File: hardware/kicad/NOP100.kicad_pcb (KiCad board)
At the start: 4 copper layers, 100 x 85 mm, 51 parts, among them CON1 MIKROBUS MODULE 0, CON2 MIKROBUS MODULE 1, J1 CAN, Q1 BSS138, Q2 BSS138, SW1 BUS, SW2 SW_Push, U1 NCS1S1205SC, U2 MCP2551-I-P, U3 Teensy_4.0, U4 74HC165, U6 NCS1S1203SC

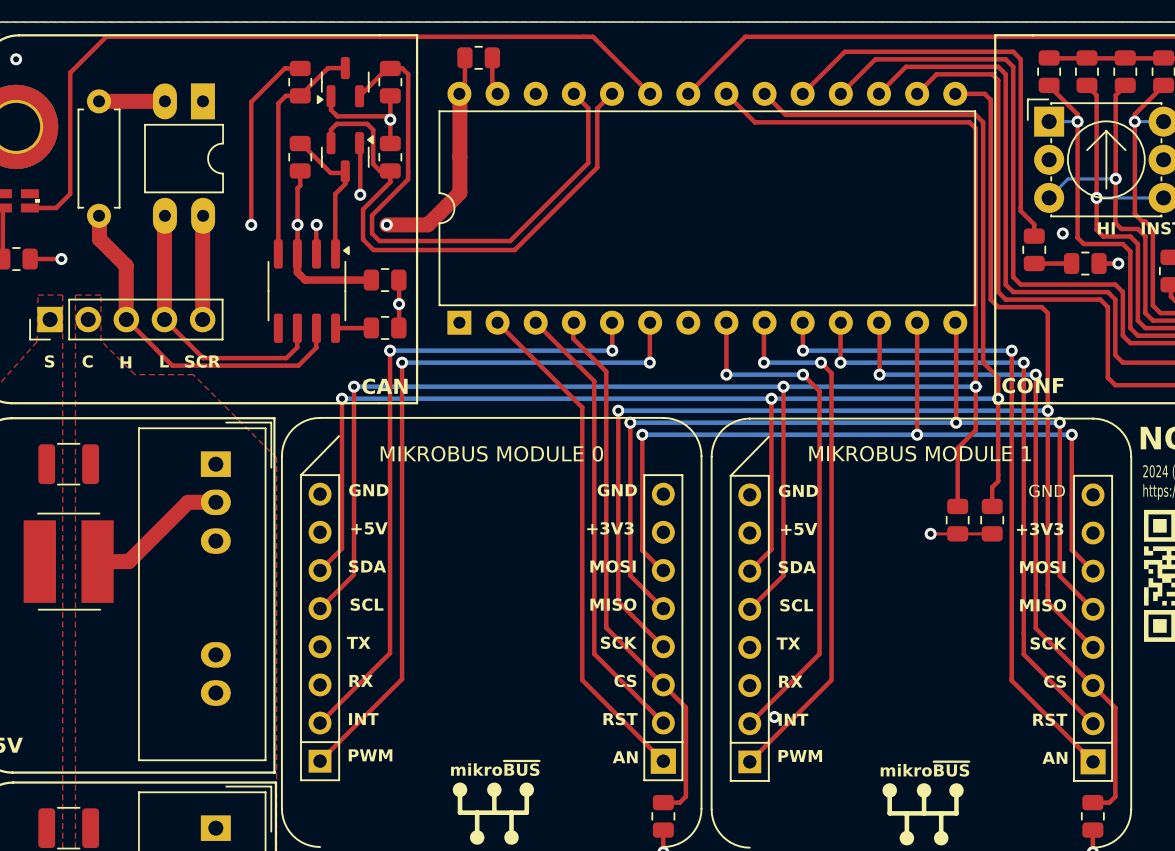
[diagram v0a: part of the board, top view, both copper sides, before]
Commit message: Add 3.3VDC alternatives.
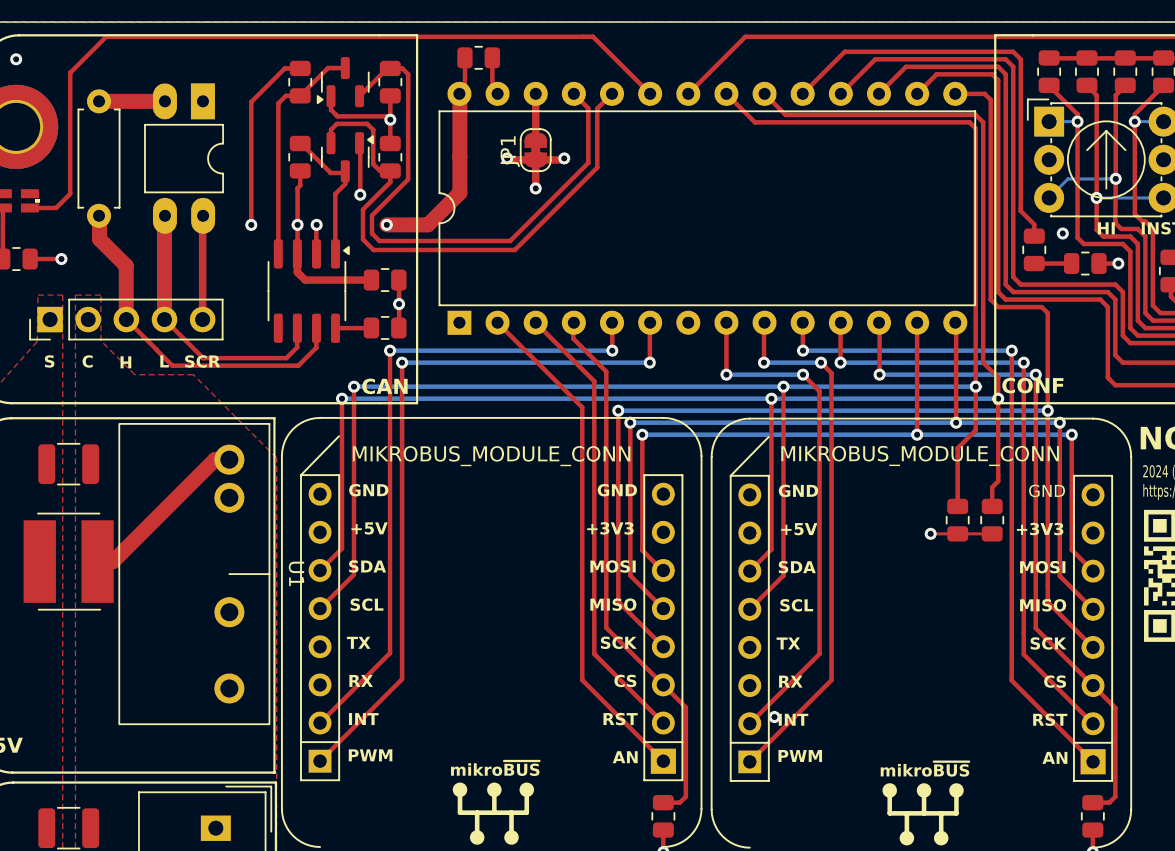
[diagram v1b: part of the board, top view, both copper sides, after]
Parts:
- added JP1: SolderJumper_2_Open, Jumper:SolderJumper-2_P1.3mm_Bridged_RoundedPad1.0x1.5mm, F.Cu at (-11.4, -34.0)
- CON1: value MIKROBUS MODULE 0 -> MIKROBUS_MODULE_CONN
- CON2: value MIKROBUS MODULE 1 -> MIKROBUS_MODULE_CONN
- U1: value NCS1S1205SC -> MURATA_MEJ2*; footprint Converter_DCDC:Converter_DCDC_Murata_NCS1SxxxxSC_THT -> pdjr:Murata-MEJ2*
- moved U1 7.38 mm to (-31.8, -5.72)
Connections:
- U1 pad 1: Net-(J1-Pin_2) -> Net-(U1-+VIN)
- U1 pad 2: Net-(U1-+VIN) -> Net-(J1-Pin_2)
- U1 pad 7: GND -> +5V
- U3 pad 26: unconnected-(U3-3.3V-Pad26) -> Net-(JP1-B)
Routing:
- net +3V3: track 33.4 -> 39.2 mm, vias 6 -> 9
- net Net-(JP1-B): track 0.00 -> 3.10 mm
- net Net-(U1-+VIN): track 9.51 -> 11.1 mm

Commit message: Library tweak
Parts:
- moved L1 8.61 mm to (-43.9, 1.94)
- moved C5 8.34 mm to (-42.6, -4.70)
- moved U1 4.75 mm to (-36.5, -5.68), turned to 90 degrees
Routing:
- net Net-(U1-+VIN): track 11.1 -> 5.45 mm
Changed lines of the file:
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@@
   )
   (footprint "pdjr:Murata-MEJ2*" (layer "F.Cu")
-    (at -31.8 -5.72 -90)
+    (at -36.55 -5.68 90)
     (property "Sheetfile" "NOP100.kicad_sch")
     (property "Sheetname" "")
@@
     (property "ki_keywords" "Murata isolated isolation dc-dc converter step-down")
     (attr through_hole)
-    (fp_text reference "U1" (at -0.01 -4.44 -90 unlocked) (layer "F.SilkS")
+    (fp_text reference "U1" (at -0.01 2.65 90 unlocked) (layer "F.Fab")
         (effects (font (size 1 1) (thickness 0.15)))
     )
-    (fp_text value "MURATA_MEJ2*" (at -0.01 3.85 -90 unlocked) (layer "F.Fab")
+    (fp_text value "MURATA_MEJ2*" (at -0.01 3.85 90 unlocked) (layer "F.Fab") hide
         (effects (font (size 1 1) (thickness 0.15)))
     )
@@
     (fp_rect (start -10 -2.67) (end 10 7.33)
       (stroke (width 0.12) (type default)) (fill none) (layer "F.SilkS"))
-    (pad "1" thru_hole circle (at -7.62 0 270) (size 2 2) (drill 1.2) (layers "*.Cu" "*.Mask")
+    (fp_rect (start -10.18 -2.87) (end 10.18 7.53)
+      (stroke (width 0.1) (type default)) (fill none) (layer "F.Fab"))
+    (pad "1" thru_hole circle (at -7.62 0 90) (size 2 2) (drill 1.2) (layers "*.Cu" "*.Mask")
       (net 7 "Net-(U1-+VIN)") (pinfunction "+VIN") (pintype "power_in"))
-    (pad "2" thru_hole circle (at -5.08 0 270) (size 2 2) (drill 1.2) (layers "*.Cu" "*.Mask")
+    (pad "2" thru_hole circle (at -5.08 0 90) (size 2 2) (drill 1.2) (layers "*.Cu" "*.Mask")
       (net 43 "Net-(J1-Pin_2)") (pinfunction "-VIN") (pintype "power_in"))
-    (pad "5" thru_hole circle (at 2.54 0 270) (size 2 2) (drill 1.2) (layers "*.Cu" "*.Mask")
+    (pad "5" thru_hole circle (at 2.54 0 90) (size 2 2) (drill 1.2) (layers "*.Cu" "*.Mask")
       (net 1 "GND") (pinfunction "-VOUT") (pintype "power_out"))
-    (pad "7" thru_hole circle (at 7.62 0 270) (size 2 2) (drill 1.2) (layers "*.Cu" "*.Mask")
+    (pad "7" thru_hole circle (at 7.62 0 90) (size 2 2) (drill 1.2) (layers "*.Cu" "*.Mask")
       (net 2 "+5V") (pinfunction "+VOUT") (pintype "power_out"))
   )
@@
   )
   (footprint "Resistor_SMD:R_1210_3225Metric" (layer "F.Cu")
-    (at -42.5 -13.04)
+    (at -42.5625 -4.7)
     (descr "Resistor SMD 1210 (3225 Metric), square (rectangular) end terminal, IPC_7351 nominal, (Body size source: IPC-SM-782 page 72, https://www.pcb-3d.com/wordpress/wp-content/uploads/ipc-sm-782a_amendment_1_and_2.pdf), generated with kicad-footprint-generator")
     (tags "resistor")
@@
   )
   (footprint "pdjr:TCK_059" (layer "F.Cu")
-    (at -42.5 -6.55 180)
+    (at -43.925 1.94 180)
     (property "Sheetfile" "NOP100.kicad_sch")
     (property "Sheetname" "")
@@
     (effects (font (size 0.8 0.8) (thickness 0.15) bold) (justify bottom))
   )
-  (gr_text "5V" (at -45.55 6.3) (layer "F.SilkS")
+  (gr_text "5V" (at -29.4 6.9) (layer "F.SilkS")
     (effects (font (size 1 1) (thickness 0.2) bold) (justify right bottom))
   )
@@
     (effects (font (size 0.8 0.8) (thickness 0.15) bold) (justify bottom))
   )
-  (gr_text "3V3" (at -44.5 29.8375) (layer "F.SilkS")
+  (gr_text "3V3" (at -44.5 30.2) (layer "F.SilkS")
     (effects (font (size 1 1) (thickness 0.2) bold) (justify right bottom))
   )
@@
   (via (at 14.9 -8.4) (size 0.8) (drill 0.4) (layers "F.Cu" "B.Cu") (free) (net 6))
   (via (at -13.3 -33.4) (size 0.8) (drill 0.4) (layers "F.Cu" "B.Cu") (free) (net 6))
-  (segment (start -39.55 -6.55) (end -40.1 -6.55) (width 1) (layer "F.Cu") (net 7))
-  (segment (start -32.76 -13.34) (end -39.55 -6.55) (width 1) (layer "F.Cu") (net 7))
-  (segment (start -31.8 -13.34) (end -32.76 -13.34) (width 1) (layer "F.Cu") (net 7))
+  (segment (start -42 1.94) (end -36.55 1.94) (width 1) (layer "F.Cu") (net 7))
   (segment (start -13.94 -22.46) (end -8.3 -16.82) (width 0.3) (layer "F.Cu") (net 8))
   (segment (start -8.3 -16.82) (end -8.3 1.34) (width 0.3) (layer "F.Cu") (net 8))
@@
       (pts
         (xy -42.05 -24.3)
+        (xy -42.2 -2.4)
+        (xy -42.2 -1)
+        (xy -41.9 4.9)
+        (xy -41.9 6.5)
         (xy -42.05 31.6)
         (xy -28.65 31.6)
@@
       (pts
         (xy -42.9 -24.3)
+        (xy -42.9 -2.4)
+        (xy -44.4 -1)
+        (xy -44.4 4.9)
+        (xy -42.9 6.5)
         (xy -42.9 31.6)
         (xy -48.7 31.6)
